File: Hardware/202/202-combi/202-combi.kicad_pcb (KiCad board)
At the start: 2 copper layers, 64 x 38 mm, 37 parts, among them J1 DM3CS-SF, P3 LEFT-201, P4 RIGHT-201, P8 202-SMART-CAM-P, U1 TXS0104, U2 TXS0104, U3 ASE-24.000MHZ-LC-T2, U5 TCA9534PWR, U6 TPS79628DCQ

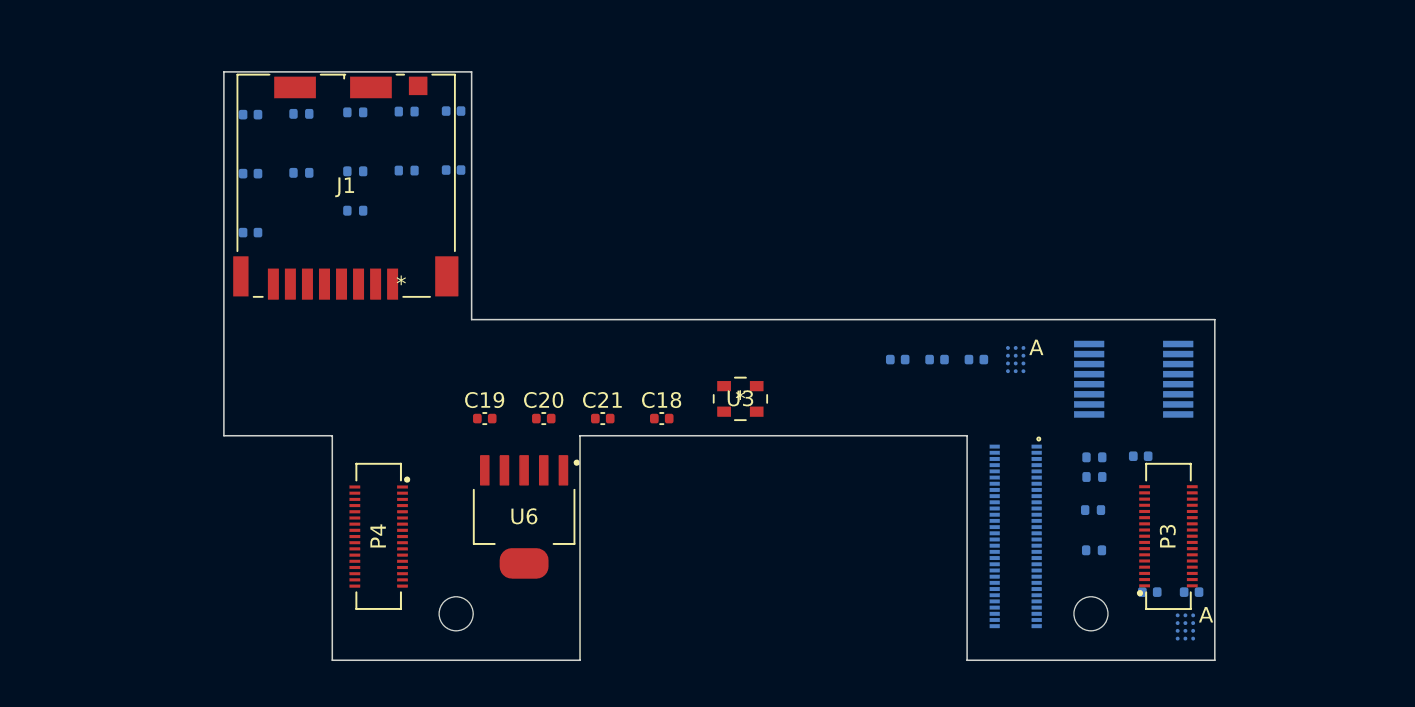
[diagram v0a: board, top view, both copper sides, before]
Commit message: Added MSP430
This will be the only expander in the future. Experiment for now
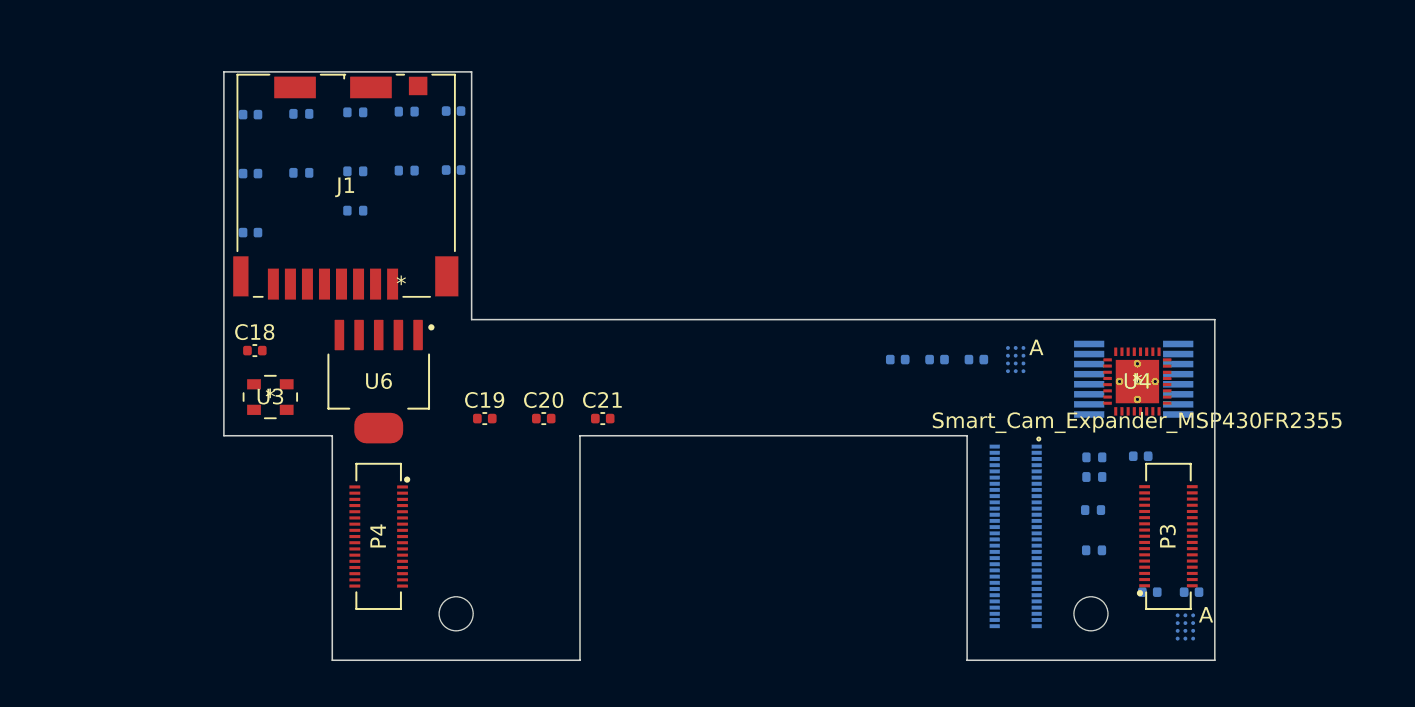
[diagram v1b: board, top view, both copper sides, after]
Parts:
- added U4: Smart_Cam_Expander_MSP430FR2355, Ziloo:MSP430FR2355TRSMR, F.Cu at (112.0, 70.0)
- moved U3 30.4 mm to (56.0, 71.0)
- moved C18 26.6 mm to (55.0, 68.0)
- moved U6 12.8 mm to (63.0, 70.0)
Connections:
- net /SYS_SCL renamed /SYS_SCL_1V8
- net /SYS_SDA renamed /SYS_SDA_1V8
- J1 pad 1: Net-(P8-Pad51) -> Net-(J1-Pad1)
- J1 pad 2: Net-(P8-Pad49) -> Net-(J1-Pad2)
- J1 pad 3: Net-(P8-Pad59) -> Net-(J1-Pad3)
- J1 pad 5: Net-(P8-Pad57) -> Net-(J1-Pad5)
- J1 pad 7: Net-(P8-Pad55) -> Net-(J1-Pad7)
- J1 pad 8: Net-(P8-Pad53) -> Net-(J1-Pad8)
- P8 pad 36: unconnected-(P8-Pad36) -> /STEM_SCL
- P8 pad 38: unconnected-(P8-Pad38) -> /STEM_SDA
- P8 pad 40: unconnected-(P8-Pad40) -> /STEM_INT
- P8 pad 47: unconnected-(P8-Pad47) -> Net-(J1-Pad9)
- P8 pad 49: Net-(P8-Pad49) -> Net-(J1-Pad2)
- P8 pad 51: Net-(P8-Pad51) -> Net-(J1-Pad1)
- P8 pad 53: Net-(P8-Pad53) -> Net-(J1-Pad8)
- P8 pad 55: Net-(P8-Pad55) -> Net-(J1-Pad7)
- P8 pad 57: Net-(P8-Pad57) -> Net-(J1-Pad5)
- P8 pad 59: Net-(P8-Pad59) -> Net-(J1-Pad3)
- R10 pad 1: Net-(P8-Pad55) -> Net-(J1-Pad8)
- R5 pad 1: Net-(P8-Pad53) -> Net-(J1-Pad1)
- R6 pad 1: Net-(P8-Pad59) -> Net-(J1-Pad2)
- R7 pad 1: Net-(P8-Pad49) -> Net-(J1-Pad3)
- R8 pad 1: Net-(P8-Pad51) -> Net-(J1-Pad5)
- R9 pad 1: Net-(P8-Pad57) -> Net-(J1-Pad7)

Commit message: Schematic clean-up
-Cleaned-up shcematics
-Added a TVS diode array to the SDCard connector.
-Impedances are calculated
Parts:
- added D1: SP7538P, Package_DFN_QFN:UDFN-9_1.0x3.8mm_P0.5mm, F.Cu at (59.7, 67.2)
- added D2: SP7538P, Package_DFN_QFN:UDFN-9_1.0x3.8mm_P0.5mm, B.Cu at (108.8, 78.8)
- moved C4 37.0 mm to (104.5, 47.7)
- moved C5 37.0 mm to (104.5, 51.5)
- moved C1 37.0 mm to (91.4, 47.9)
- moved C2 37.0 mm to (91.4, 51.7)
- moved C3 37.0 mm to (91.4, 55.5)
- moved R10 37.0 mm to (94.6, 51.7)
- moved R11 37.0 mm to (98.1, 54.1)
- moved R5 37.0 mm to (101.4, 51.5)
- moved R6 37.0 mm to (101.4, 47.7)
- moved R7 37.0 mm to (98.1, 47.7)
- moved R8 37.0 mm to (98.1, 51.6)
- moved R9 37.0 mm to (94.6, 47.8)
- moved U6 21.4 mm to (43.9, 60.4)
- moved R1 15.7 mm to (124.8, 77.3)
- moved R3 15.7 mm to (124.7, 80.7)
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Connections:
- net Net-(J1-Pad1) renamed /DAT2
- net Net-(J1-Pad2) renamed /DAT3
- net Net-(J1-Pad3) renamed /CMD
- net Net-(J1-Pad5) renamed /CLK
- net Net-(J1-Pad7) renamed /DAT0
- net Net-(J1-Pad8) renamed /DAT1
- net Net-(J1-Pad9) renamed /CDS
- net Net-(P3-Pad12) renamed /I2C_SCL_1v8_LEFT
- net Net-(P3-Pad13) renamed /I2C_SDA_1v8_LEFT
- net Net-(P3-Pad14) renamed /I2S_SCK
- net Net-(P3-Pad15) renamed /I2S_LRCLK
- net Net-(P3-Pad16) renamed /I2S_D1
- net Net-(P3-Pad17) renamed /I2S_D2
- net Net-(P3-Pad18) renamed /CSI_L_RX_CLK_N
- net Net-(P3-Pad19) renamed /CSI_L_RX_CLK_P
- net Net-(P3-Pad21) renamed /CSI_L_RX_D2_N
- net Net-(P3-Pad22) renamed /CSI_L_RX_D2_P
- net Net-(P3-Pad24) renamed /CSI_L_RX_D1_N
- net Net-(P3-Pad25) renamed /CSI_L_RX_D1_P
- net Net-(P3-Pad27) renamed /CSI_L_RX_D0_N
- net Net-(P3-Pad28) renamed /CSI_L_RX_D0_P
- net Net-(P4-Pad12) renamed /I2C_SCL_1v8_RIGHT
- net Net-(P4-Pad13) renamed /I2C_SDA_1v8_RIGHT
- net Net-(P4-Pad18) renamed /CSI_R_RX_CLK_N
- net Net-(P4-Pad19) renamed /CSI_R_RX_CLK_P
- net Net-(P4-Pad24) renamed /CSI_R_RX_D1_N
- net Net-(P4-Pad25) renamed /CSI_R_RX_D1_P
- net Net-(P4-Pad27) renamed /CSI_R_RX_D0_N
- net Net-(P4-Pad28) renamed /CSI_R_RX_D0_P
- net Net-(P8-Pad45) renamed /SYS_EX_nINT
- P4 pad 20: GND -> unconnected-(P4-Pad20)
- P8 pad 39: Net-(P8-Pad39) -> /OE_CAM
- P8 pad 42: Net-(P8-Pad42) -> /SYS_SCL
- P8 pad 44: Net-(P8-Pad44) -> /SYS_SDA
- U1 pad B3: Net-(P8-Pad39) -> /OE_CAM
- U2 pad A2: /SYS_SDA_1V8 -> +1V8
- U2 pad A3: /SYS_SCL_1V8 -> unconnected-(U2-PadA3)
- U2 pad B1: +1V8 -> /SYS_SDA
- U2 pad B3: Net-(P8-Pad39) -> /SYS_SDA_1V8
- U2 pad C1: unconnected-(U2-PadC1) -> /SYS_SCL
- U2 pad C2: Net-(P8-Pad44) -> /OE_CAM
- U2 pad C3: Net-(P8-Pad42) -> /SYS_SCL_1V8
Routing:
- net /CDS: track 0.00 -> 22.5 mm
- net GND: track 0.00 -> 10.1 mm, vias 0 -> 6
- net /DAT1: track 0.00 -> 5.48 mm
- net /DAT3: track 0.00 -> 5.26 mm
- net /DAT2: track 0.00 -> 4.85 mm
- net /DAT0: track 0.00 -> 4.53 mm
- net +3.3V: track 0.00 -> 4.21 mm
- net /CLK: track 0.00 -> 4.09 mm
- net /CMD: track 0.00 -> 3.55 mm

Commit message: Add files via upload
Mostly Routed
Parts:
- removed D1, D2: SP7538P, Package_DFN_QFN:UDFN-9_1.0x3.8mm_P0.5mm
- moved C4 37.0 mm to (67.8, 52.5)
- moved C5 37.0 mm to (67.8, 56.3)
- moved C1 37.0 mm to (54.7, 52.8)
- moved C2 37.0 mm to (54.7, 56.6)
- moved C3 37.0 mm to (54.7, 60.4)
- moved R10 37.0 mm to (58.0, 56.5)
- moved R11 37.0 mm to (61.5, 59.0)
- moved R5 37.0 mm to (64.8, 56.4)
- moved R6 37.0 mm to (64.8, 52.6)
- moved R7 37.0 mm to (61.5, 52.6)
- moved R8 37.0 mm to (61.5, 56.4)
- moved R9 37.0 mm to (58.0, 52.7)
- moved U6 21.4 mm to (63.0, 70.0)
- moved R1 15.7 mm to (109.2, 74.9)
- moved R3 15.7 mm to (109.1, 78.3)
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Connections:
- net /CDS renamed Net-(J1-Pad9)
- net /CLK renamed Net-(J1-Pad5)
- net /CMD renamed Net-(J1-Pad3)
- net /CSI_L_RX_CLK_N renamed Net-(P3-Pad18)
- net /CSI_L_RX_CLK_P renamed Net-(P3-Pad19)
- net /CSI_L_RX_D0_N renamed Net-(P3-Pad27)
- net /CSI_L_RX_D0_P renamed Net-(P3-Pad28)
- net /CSI_L_RX_D1_N renamed Net-(P3-Pad24)
- net /CSI_L_RX_D1_P renamed Net-(P3-Pad25)
- net /CSI_L_RX_D2_N renamed Net-(P3-Pad21)
- net /CSI_L_RX_D2_P renamed Net-(P3-Pad22)
- net /CSI_R_RX_CLK_N renamed Net-(P4-Pad18)
- net /CSI_R_RX_CLK_P renamed Net-(P4-Pad19)
- net /CSI_R_RX_D0_N renamed Net-(P4-Pad27)
- net /CSI_R_RX_D0_P renamed Net-(P4-Pad28)
- net /CSI_R_RX_D1_N renamed Net-(P4-Pad24)
- net /CSI_R_RX_D1_P renamed Net-(P4-Pad25)
- net /DAT0 renamed Net-(J1-Pad7)
- net /DAT1 renamed Net-(J1-Pad8)
- net /DAT2 renamed Net-(J1-Pad1)
- net /DAT3 renamed Net-(J1-Pad2)
- net /I2C_SCL_1v8_LEFT renamed Net-(P3-Pad12)
- net /I2C_SCL_1v8_RIGHT renamed Net-(P4-Pad12)
- net /I2C_SDA_1v8_LEFT renamed Net-(P3-Pad13)
- net /I2C_SDA_1v8_RIGHT renamed Net-(P4-Pad13)
- net /I2S_D1 renamed Net-(P3-Pad16)
- net /I2S_D2 renamed Net-(P3-Pad17)
- net /I2S_LRCLK renamed Net-(P3-Pad15)
- net /I2S_SCK renamed Net-(P3-Pad14)
- net /SYS_EX_nINT renamed Net-(P8-Pad45)
- P4 pad 20: unconnected-(P4-Pad20) -> GND
- P8 pad 39: /OE_CAM -> Net-(P8-Pad39)
- P8 pad 42: /SYS_SCL -> Net-(P8-Pad42)
- P8 pad 44: /SYS_SDA -> Net-(P8-Pad44)
- U1 pad B3: /OE_CAM -> Net-(P8-Pad39)
- U2 pad A2: +1V8 -> /SYS_SDA_1V8
- U2 pad A3: unconnected-(U2-PadA3) -> /SYS_SCL_1V8
- U2 pad B1: /SYS_SDA -> +1V8
- U2 pad B3: /SYS_SDA_1V8 -> Net-(P8-Pad39)
- U2 pad C1: /SYS_SCL -> unconnected-(U2-PadC1)
- U2 pad C2: /OE_CAM -> Net-(P8-Pad44)
- U2 pad C3: /SYS_SCL_1V8 -> Net-(P8-Pad42)
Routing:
- net Net-(J1-Pad9): track 22.5 -> 0.00 mm
- net GND: track 10.1 -> 0.00 mm, vias 6 -> 0
- net Net-(J1-Pad8): track 5.48 -> 0.00 mm
- net Net-(J1-Pad2): track 5.26 -> 0.00 mm
- net Net-(J1-Pad1): track 4.85 -> 0.00 mm
- net Net-(J1-Pad7): track 4.53 -> 0.00 mm
- net +3.3V: track 4.21 -> 0.00 mm
- net Net-(J1-Pad5): track 4.09 -> 0.00 mm
- net Net-(J1-Pad3): track 3.55 -> 0.00 mm

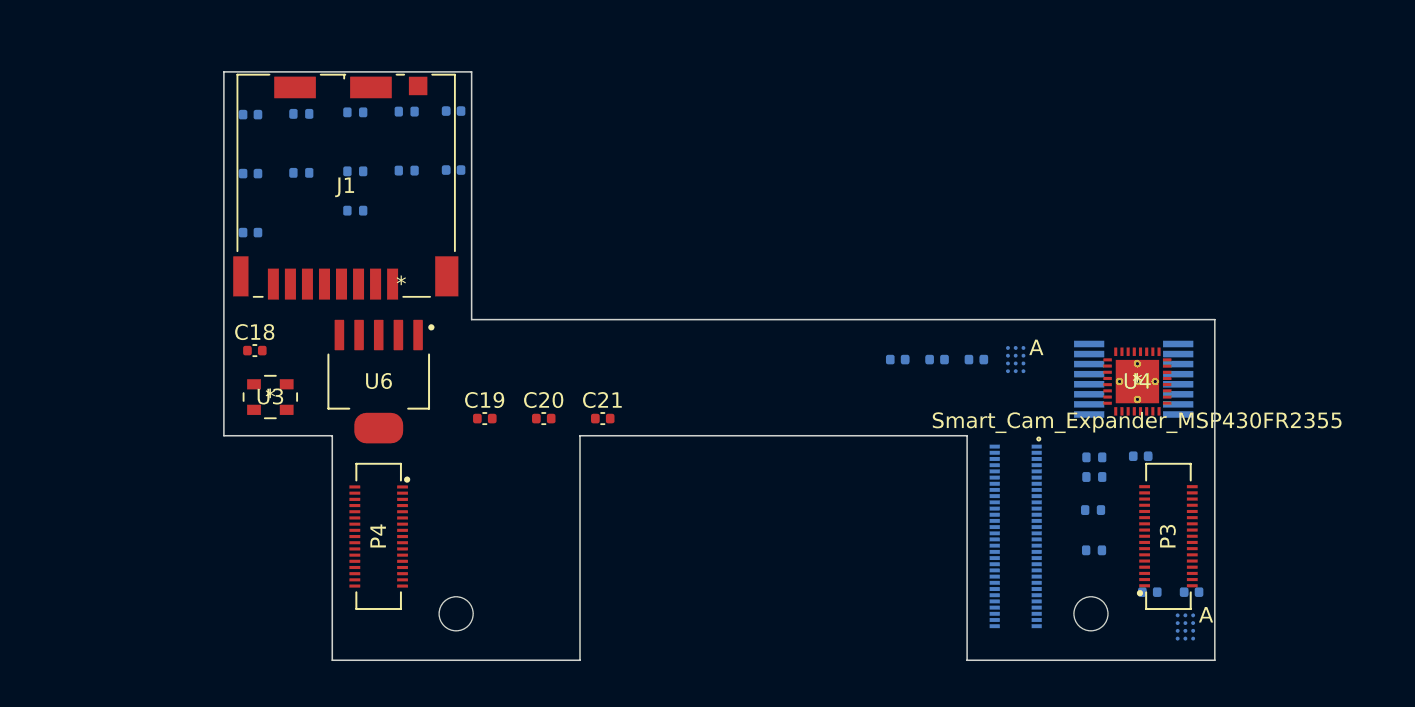
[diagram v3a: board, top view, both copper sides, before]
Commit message: Add files via upload
ROuting completed, differential pairs are length matched and tuned
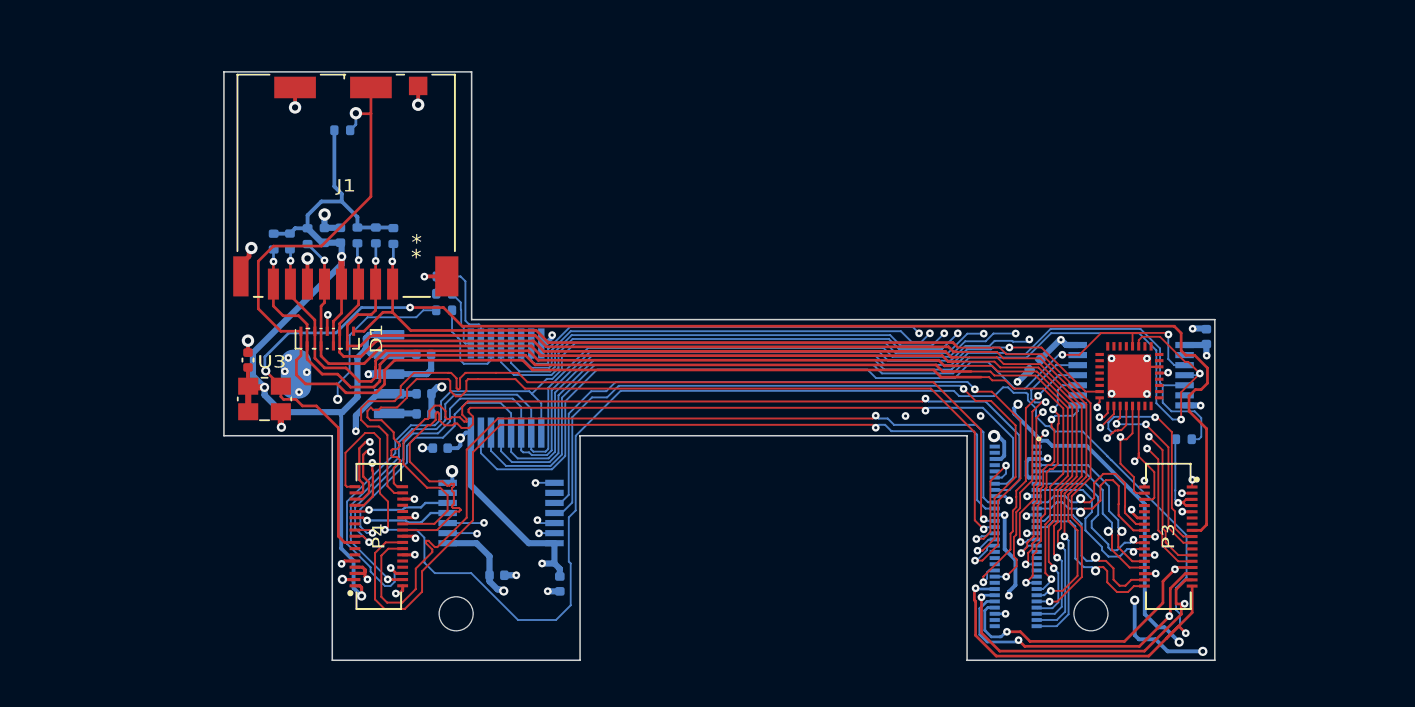
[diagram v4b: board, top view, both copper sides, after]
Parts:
- removed C14, C3, C4, C5: 100nF, Capacitor_SMD:C_0402_1005Metric
- added D1: SP7538P, Package_DFN_QFN:UDFN-9_1.0x3.8mm_P0.5mm, F.Cu at (59.7, 67.2)
- C19, C20, C21, U6: moved to B.Cu
- P3, P4: footprint Ziloo:HIROSE_DF40C-34DS-0.4V(51) -> Ziloo:HIROSE_DF40C-34DS-0.4V(51)_corrected
- U1, U2: value TXS0104 -> TXS0104EPWR; footprint Ziloo:TXS0104EYZTR -> Package_SO:SSOP-14_5.3x6.2mm_P0.65mm
- moved R4 45.1 mm to (67.2, 64.3)
- moved U1 44.8 mm to (70.9, 78.5), turned to 0 degrees
- moved R3 44.5 mm to (67.3, 63.2)
- moved R1 43.1 mm to (67.2, 65.4), turned to 0 degrees
- moved C11 42.2 mm to (70.6, 82.5), turned to 0 degrees
- moved C9 40.8 mm to (74.7, 83.1), turned to -90 degrees
- moved U5 40.5 mm to (71.2, 70.4), turned to -90 degrees
- moved C17 30.1 mm to (67.0, 74.3), turned to 0 degrees
- moved C6 14.9 mm to (116.5, 67.1), turned to 90 degrees
- moved C21 11.7 mm to (65.9, 70.8)
- moved C1 9.72 mm to (60.5, 60.5), turned to -90 degrees
- moved R9 8.27 mm to (57.3, 61.0), turned to 90 degrees
- moved R6 8.24 mm to (62.8, 60.6), turned to 90 degrees
- moved R7 7.95 mm to (61.6, 60.6), turned to 90 degrees
- moved C20 7.74 mm to (65.9, 72.1)
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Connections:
- net Net-(J1-Pad1) renamed /DAT2
- net Net-(J1-Pad2) renamed /DAT3
- net Net-(J1-Pad3) renamed /CMD
- net Net-(J1-Pad5) renamed /CLK
- net Net-(J1-Pad7) renamed /DAT0
- net Net-(J1-Pad8) renamed /DAT1
- net Net-(J1-Pad9) renamed /CDS
- net Net-(P3-Pad14) renamed /I2S_SCK
- net Net-(P3-Pad15) renamed /I2S_LRCLK
- net Net-(P3-Pad16) renamed /I2S_D1
- net Net-(P3-Pad17) renamed /I2S_D2
- net Net-(P3-Pad18) renamed /CSI_L_RX_CLK_N
- net Net-(P3-Pad19) renamed /CSI_L_RX_CLK_P
- net Net-(P3-Pad21) renamed /CSI_L_RX_D2_N
- net Net-(P3-Pad22) renamed /CSI_L_RX_D2_P
- net Net-(P3-Pad24) renamed /CSI_L_RX_D1_N
- net Net-(P3-Pad25) renamed /CSI_L_RX_D1_P
- net Net-(P3-Pad27) renamed /CSI_L_RX_D0_N
- net Net-(P3-Pad28) renamed /CSI_L_RX_D0_P
- net Net-(P4-Pad18) renamed /CSI_R_RX_CLK_N
- net Net-(P4-Pad19) renamed /CSI_R_RX_CLK_P
- net Net-(P4-Pad24) renamed /CSI_R_RX_D1_N
- net Net-(P4-Pad25) renamed /CSI_R_RX_D1_P
- net Net-(P4-Pad27) renamed /CSI_R_RX_D0_N
- net Net-(P4-Pad28) renamed /CSI_R_RX_D0_P
- P3 pad 12: Net-(P3-Pad12) -> /I2C_SCL_1v8_LEFT
- P3 pad 13: Net-(P3-Pad13) -> /I2C_SDA_1v8_LEFT
- P4 pad 12: Net-(P4-Pad12) -> /I2C_SCL_1v8_RIGHT
- P4 pad 13: Net-(P4-Pad13) -> /I2C_SDA_1v8_RIGHT
- P8 pad 39: Net-(P8-Pad39) -> /OE_CAM
- P8 pad 42: Net-(P8-Pad42) -> /SYS_SCL
- P8 pad 44: Net-(P8-Pad44) -> /SYS_SDA
- P8 pad 45: Net-(P8-Pad45) -> /SYS_EX_nINT
- U4 pad 33: unconnected-(U4-Pad33) -> GND
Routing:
- net +3.3V: track 0.00 -> 214.1 mm, vias 0 -> 11
- net +1V8: track 0.00 -> 179.2 mm, vias 0 -> 9
- net /I2S_D2: track 0.00 -> 114.7 mm, vias 0 -> 3
- net +2V8: track 0.00 -> 109.8 mm, vias 0 -> 5
- net /I2S_D1: track 0.00 -> 105.2 mm, vias 0 -> 3
- net /I2S_LRCLK: track 0.00 -> 97.8 mm, vias 0 -> 3
- net /CDS: track 0.00 -> 93.3 mm, vias 0 -> 2
- net /EXTCLK: track 0.00 -> 92.6 mm, vias 0 -> 2
- net /I2S_SCK: track 0.00 -> 90.9 mm, vias 0 -> 3
- net /DAT0: track 0.00 -> 76.5 mm, vias 0 -> 2
- net /DAT1: track 0.00 -> 76.2 mm, vias 0 -> 2
- net /CLK: track 0.00 -> 74.9 mm, vias 0 -> 2
- net /CMD: track 0.00 -> 74.2 mm, vias 0 -> 2
- net /DAT3: track 0.00 -> 73.0 mm, vias 0 -> 2
- net /RIGHT_PWRDN: track 0.00 -> 72.2 mm, vias 0 -> 3
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- added copper zone on In1.Cu, net GND
- added copper zone on In2.Cu, net GND
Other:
- copper layers 2 -> 4
